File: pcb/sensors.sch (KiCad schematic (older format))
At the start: 0 parts

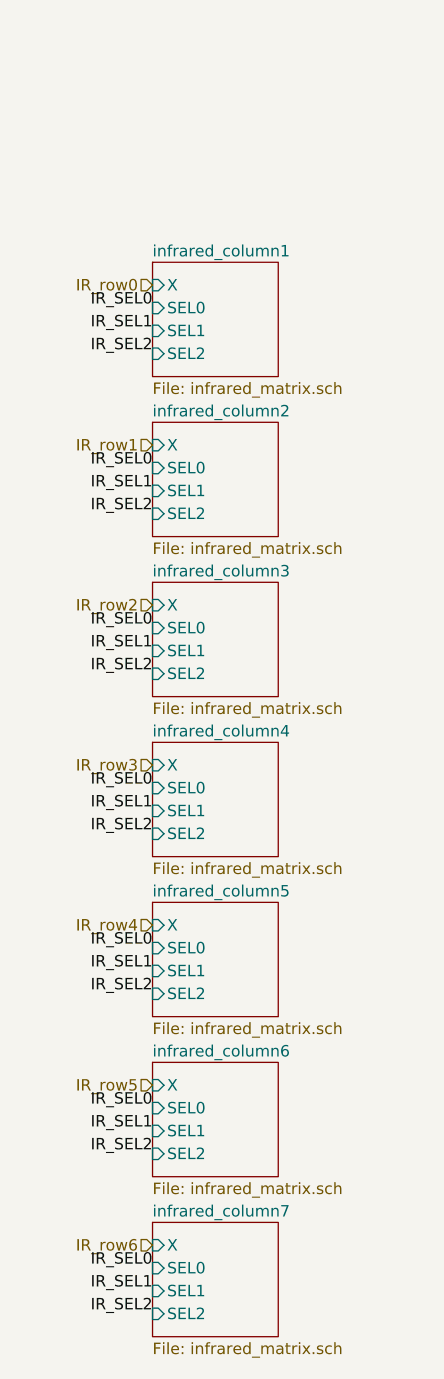
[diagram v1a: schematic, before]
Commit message: Use Buses for IR sensors
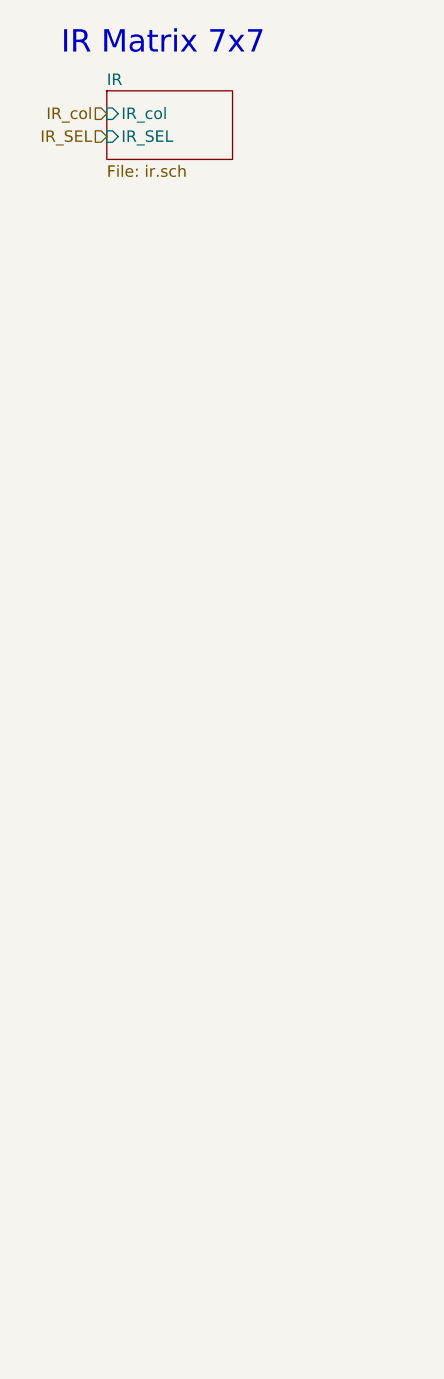
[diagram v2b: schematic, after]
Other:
- note added: "IR Matrix 7x7"
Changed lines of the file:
@@
 $Descr A4 11693 8268
 encoding utf-8
-Sheet 3 17
+Sheet 3 19
 Title ""
 Date ""
@@
 $EndDescr
 $Sheet
-S 10250 1700 550  500
-U 5D2CABF0
-F0 "infrared_column1" 50
-F1 "infrared_matrix.sch" 50
-F2 "X" I L 10250 1800 50
-F3 "SEL0" I L 10250 1900 50
-F4 "SEL1" I L 10250 2000 50
-F5 "SEL2" I L 10250 2100 50
+S 10050 950  550  300
+U 5D25183D
+F0 "IR" 50
+F1 "ir.sch" 50
+F2 "IR_SEL" I L 10050 1150 50
+F3 "IR_col" I L 10050 1050 50
 $EndSheet
-$Sheet
-S 10250 2400 550  500
-U 5D2E88EC
-F0 "infrared_column2" 50
-F1 "infrared_matrix.sch" 50
-F2 "X" I L 10250 2500 50
-F3 "SEL0" I L 10250 2600 50
-F4 "SEL1" I L 10250 2700 50
-F5 "SEL2" I L 10250 2800 50
-$EndSheet
-$Sheet
-S 10250 3100 550  500
-U 5D2E8906
-F0 "infrared_column3" 50
-F1 "infrared_matrix.sch" 50
-F2 "X" I L 10250 3200 50
-F3 "SEL0" I L 10250 3300 50
-F4 "SEL1" I L 10250 3400 50
-F5 "SEL2" I L 10250 3500 50
-$EndSheet
-$Sheet
-S 10250 3800 550  500
-U 5D2E8934
-F0 "infrared_column4" 50
-F1 "infrared_matrix.sch" 50
-F2 "X" I L 10250 3900 50
-F3 "SEL0" I L 10250 4000 50
-F4 "SEL1" I L 10250 4100 50
-F5 "SEL2" I L 10250 4200 50
-$EndSheet
-$Sheet
-S 10250 4500 550  500
-U 5D2E8986
-F0 "infrared_column5" 50
-F1 "infrared_matrix.sch" 50
-F2 "X" I L 10250 4600 50
-F3 "SEL0" I L 10250 4700 50
-F4 "SEL1" I L 10250 4800 50
-F5 "SEL2" I L 10250 4900 50
-$EndSheet
-$Sheet
-S 10250 5200 550  500
-U 5D2E89D4
-F0 "infrared_column6" 50
-F1 "infrared_matrix.sch" 50
-F2 "X" I L 10250 5300 50
-F3 "SEL0" I L 10250 5400 50
-F4 "SEL1" I L 10250 5500 50
-F5 "SEL2" I L 10250 5600 50
-$EndSheet
-$Sheet
-S 10250 5900 550  500
-U 5D2E8A06
-F0 "infrared_column7" 50
-F1 "infrared_matrix.sch" 50
-F2 "X" I L 10250 6000 50
-F3 "SEL0" I L 10250 6100 50
-F4 "SEL1" I L 10250 6200 50
-F5 "SEL2" I L 10250 6300 50
-$EndSheet
-Text Label 10250 1900 2    50   ~ 0
-IR_SEL0
-Text Label 10250 2000 2    50   ~ 0
-IR_SEL1
-Text Label 10250 2100 2    50   ~ 0
-IR_SEL2
-Text Label 10250 2600 2    50   ~ 0
-IR_SEL0
-Text Label 10250 2700 2    50   ~ 0
-IR_SEL1
-Text Label 10250 2800 2    50   ~ 0
-IR_SEL2
-Text Label 10250 3300 2    50   ~ 0
-IR_SEL0
-Text Label 10250 3400 2    50   ~ 0
-IR_SEL1
-Text Label 10250 3500 2    50   ~ 0
-IR_SEL2
-Text Label 10250 4000 2    50   ~ 0
-IR_SEL0
-Text Label 10250 4100 2    50   ~ 0
-IR_SEL1
-Text Label 10250 4200 2    50   ~ 0
-IR_SEL2
-Text Label 10250 4700 2    50   ~ 0
-IR_SEL0
-Text Label 10250 4800 2    50   ~ 0
-IR_SEL1
-Text Label 10250 4900 2    50   ~ 0
-IR_SEL2
-Text Label 10250 5400 2    50   ~ 0
-IR_SEL0
-Text Label 10250 5500 2    50   ~ 0
-IR_SEL1
-Text Label 10250 5600 2    50   ~ 0
-IR_SEL2
-Text Label 10250 6100 2    50   ~ 0
-IR_SEL0
-Text Label 10250 6200 2    50   ~ 0
-IR_SEL1
-Text Label 10250 6300 2    50   ~ 0
-IR_SEL2
-Text HLabel 10250 2500 0    50   Input ~ 0
-IR_row1
-Text HLabel 10250 3200 0    50   Input ~ 0
-IR_row2
-Text HLabel 10250 1800 0    50   Input ~ 0
-IR_row0
-Text HLabel 10250 3900 0    50   Input ~ 0
-IR_row3
-Text HLabel 10250 4600 0    50   Input ~ 0
-IR_row4
-Text HLabel 10250 5300 0    50   Input ~ 0
-IR_row5
-Text HLabel 10250 6000 0    50   Input ~ 0
-IR_row6
+Text Notes 9850 800  0    98   ~ 0
+IR Matrix 7x7
+Text HLabel 10050 1050 0    50   Input ~ 0
+IR_col
+Text HLabel 10050 1150 0    50   Input ~ 0
+IR_SEL
 $EndSCHEMATC

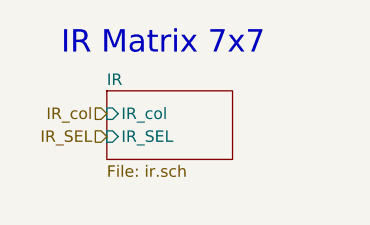
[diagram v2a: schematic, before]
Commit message: IR matrix complete minus control transistor
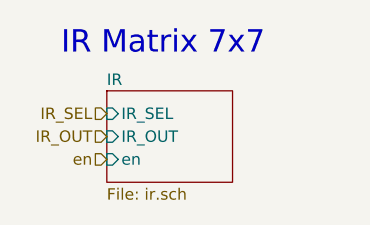
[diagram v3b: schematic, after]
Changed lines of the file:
@@
 $Descr A4 11693 8268
 encoding utf-8
-Sheet 3 19
+Sheet 3 12
 Title ""
 Date ""
@@
 $EndDescr
 $Sheet
-S 10050 950  550  300
+S 10050 950  550  400
 U 5D25183D
 F0 "IR" 50
 F1 "ir.sch" 50
-F2 "IR_SEL" I L 10050 1150 50
-F3 "IR_col" I L 10050 1050 50
+F2 "IR_SEL" I L 10050 1050 50
+F3 "IR_OUT" I L 10050 1150 50
+F4 "en" I L 10050 1250 50
 $EndSheet
 Text Notes 9850 800  0    98   ~ 0
 IR Matrix 7x7
 Text HLabel 10050 1050 0    50   Input ~ 0
-IR_col
+IR_SEL
 Text HLabel 10050 1150 0    50   Input ~ 0
-IR_SEL
+IR_OUT
+Text HLabel 10050 1250 0    50   Input ~ 0
+en
 $EndSCHEMATC
